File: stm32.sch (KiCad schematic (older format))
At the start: 30 parts, among them U3 STM32F205RBTx, U4 OLED_0.96\"_SSD1306, Y2 8M

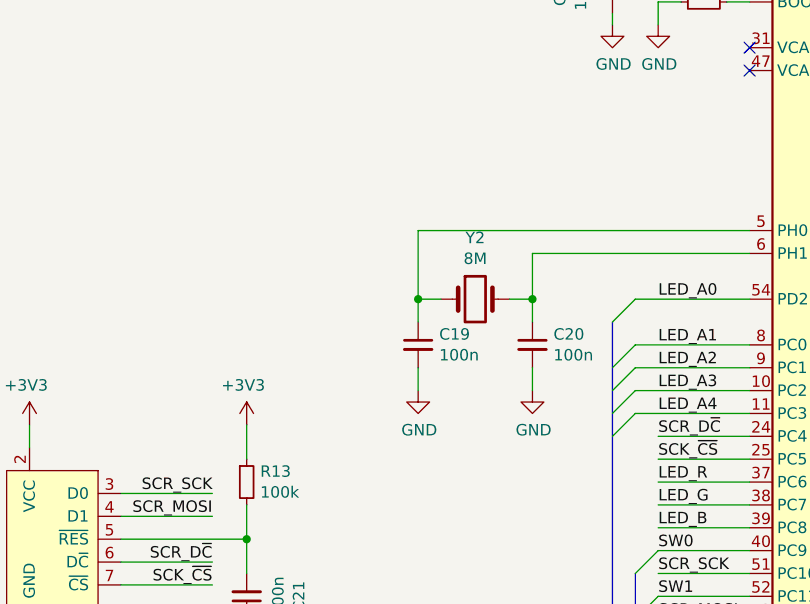
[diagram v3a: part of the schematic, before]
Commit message: sch, pcb: Fix hub startup and use smaller crystals
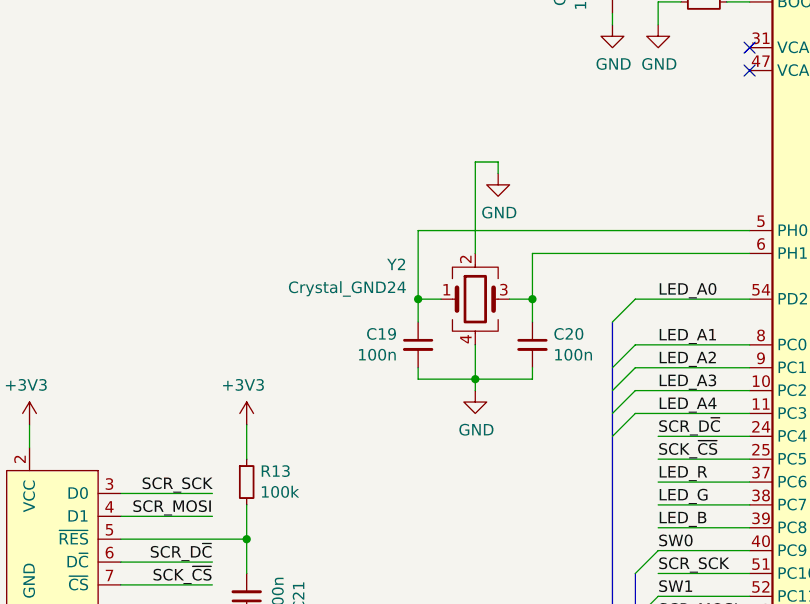
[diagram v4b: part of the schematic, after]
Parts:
- removed Y2: 8M, Crystal:Crystal_HC49-4H_Vertical, symbol Device:Crystal
- added Y2: Crystal_GND24, Crystal:Crystal_SMD_3225-4Pin_3.2x2.5mm, symbol Device:Crystal_GND24
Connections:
- net GND: now also Y2.2, Y2.4
- net at C19.1, U3.5 (PH0): now also Y2.1
- net at C20.1, U3.6 (PH1): now also Y2.3
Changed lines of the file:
@@
 	5000 3750 4050 3750
 Wire Wire Line
-	4050 4250 4050 4350
-Wire Wire Line
-	3550 4250 3550 4350
+	3800 4150 3800 4300
 $Comp
 L power:GND #PWR?
 U 1 1 5DFC7A41
-P 3550 4350
+P 3800 4350
 AR Path="/5DF7E971/5DFC7A41" Ref="#PWR?"  Part="1"
 AR Path="/5DFC2583/5DFC7A41" Ref="#PWR0123"  Part="1"
-F 0 "#PWR0123" H 3550 4100 50  0001 C CNN
-F 1 "GND" H 3555 4177 50  0000 C CNN
-F 2 "" H 3550 4350 50  0001 C CNN
-F 3 "" H 3550 4350 50  0001 C CNN
-	1    3550 4350
-	1    0    0    -1
-$EndComp
-$Comp
-L power:GND #PWR?
-U 1 1 5DFC7A3B
-P 4050 4350
-AR Path="/5DF7E971/5DFC7A3B" Ref="#PWR?"  Part="1"
-AR Path="/5DFC2583/5DFC7A3B" Ref="#PWR0122"  Part="1"
-F 0 "#PWR0122" H 4050 4100 50  0001 C CNN
-F 1 "GND" H 4055 4177 50  0000 C CNN
-F 2 "" H 4050 4350 50  0001 C CNN
-F 3 "" H 4050 4350 50  0001 C CNN
-	1    4050 4350
+F 0 "#PWR0123" H 3800 4100 50  0001 C CNN
+F 1 "GND" H 3805 4177 50  0000 C CNN
+F 2 "" H 3800 4350 50  0001 C CNN
+F 3 "" H 3800 4350 50  0001 C CNN
+	1    3800 4350
 	1    0    0    -1
 $EndComp
@@
 AR Path="/5DF7E971/5DFC7A25" Ref="C?"  Part="1"
 AR Path="/5DFC2583/5DFC7A25" Ref="C19"  Part="1"
-F 0 "C19" H 3458 4196 50  0000 R CNN
-F 1 "100n" H 3458 4105 50  0000 R CNN
+F 0 "C19" H 3642 4196 50  0000 L CNN
+F 1 "100n" H 3642 4105 50  0000 L CNN
 F 2 "Capacitor_SMD:C_0603_1608Metric" H 3550 4150 50  0001 C CNN
 F 3 "~" H 3550 4150 50  0001 C CNN
 	1    3550 4150
 	-1   0    0    -1
-$EndComp
-$Comp
-L Device:Crystal Y?
-U 1 1 5DFC7A1F
-P 3800 3950
-AR Path="/5DF7E971/5DFC7A1F" Ref="Y?"  Part="1"
-AR Path="/5DFC2583/5DFC7A1F" Ref="Y2"  Part="1"
-F 0 "Y2" H 3800 4218 50  0000 C CNN
-F 1 "8M" H 3800 4127 50  0000 C CNN
-F 2 "Crystal:Crystal_HC49-4H_Vertical" H 3800 3950 50  0001 C CNN
-F 3 "~" H 3800 3950 50  0001 C CNN
-	1    3800 3950
-	1    0    0    -1
 $EndComp
 Wire Wire Line
@@
 Wire Wire Line
 	1350 1200 1450 1200
+$Comp
+L Device:Crystal_GND24 Y?
+U 1 1 5EEC6C7F
+P 3800 3950
+AR Path="/5DF7E971/5EEC6C7F" Ref="Y?"  Part="1"
+AR Path="/5DFC2583/5EEC6C7F" Ref="Y2"  Part="1"
+F 0 "Y2" H 3500 4100 50  0000 R CNN
+F 1 "Crystal_GND24" H 3500 4000 50  0000 R CNN
+F 2 "Crystal:Crystal_SMD_3225-4Pin_3.2x2.5mm" H 3800 3950 50  0001 C CNN
+F 3 "~" H 3800 3950 50  0001 C CNN
+	1    3800 3950
+	1    0    0    -1
+$EndComp
+Wire Wire Line
+	3550 4250 3550 4300
+Wire Wire Line
+	3550 4300 3800 4300
+Connection ~ 3800 4300
+Wire Wire Line
+	3800 4300 3800 4350
+Wire Wire Line
+	3800 4300 4050 4300
+Wire Wire Line
+	4050 4300 4050 4250
+$Comp
+L power:GND #PWR?
+U 1 1 5EF1AE7A
+P 3900 3400
+AR Path="/5DF7E971/5EF1AE7A" Ref="#PWR?"  Part="1"
+AR Path="/5DFC2583/5EF1AE7A" Ref="#PWR062"  Part="1"
+F 0 "#PWR062" H 3900 3150 50  0001 C CNN
+F 1 "GND" H 3905 3227 50  0000 C CNN
+F 2 "" H 3900 3400 50  0001 C CNN
+F 3 "" H 3900 3400 50  0001 C CNN
+	1    3900 3400
+	1    0    0    -1
+$EndComp
+Wire Wire Line
+	3800 3750 3800 3350
+Wire Wire Line
+	3800 3350 3900 3350
+Wire Wire Line
+	3900 3350 3900 3400
 Wire Bus Line
 	4400 4050 4400 6450
